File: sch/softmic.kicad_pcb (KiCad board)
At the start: 2 copper layers, 101.6 x 62.2 mm, 87 parts, among them J1 USB-C Connector, J3 XLR-OUT, J4 AudioJack 3.5mm, P1 4V1, P10 none, P2 4V1, P3 4V1, P4 4V1, P5 4V1, P6 VccPad, P7 none, P8 none, P9 none, Q1 MCP1812BT-033, Q10 ESP32-WROOM, Q11 BC847BS-TP, Q2 MMBFJ201, Q3 CH340G, Q4 BSS64AT116, Q5 OPA1671, Q6 OPA1671, Q7 BQ21040, Q8 MAX11613, Q9 Oled_128_32, SW1 RST, Y1 12MHz

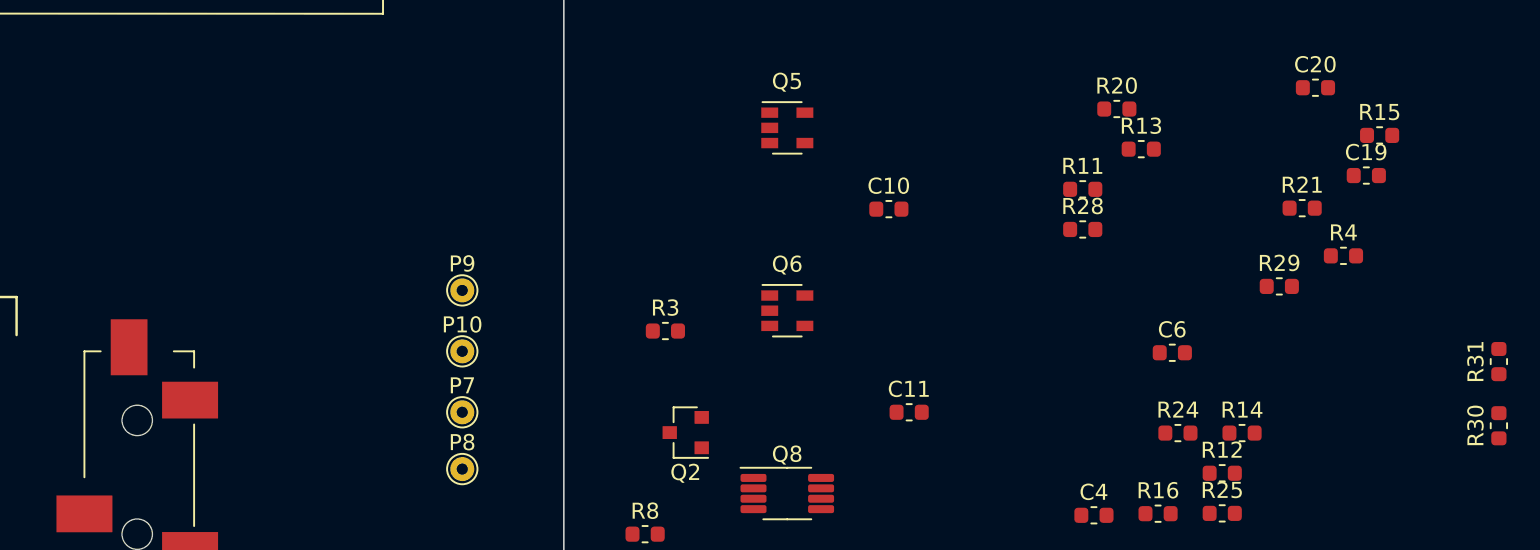
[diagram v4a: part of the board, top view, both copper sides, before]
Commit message: added small headphone volume potentiomenter
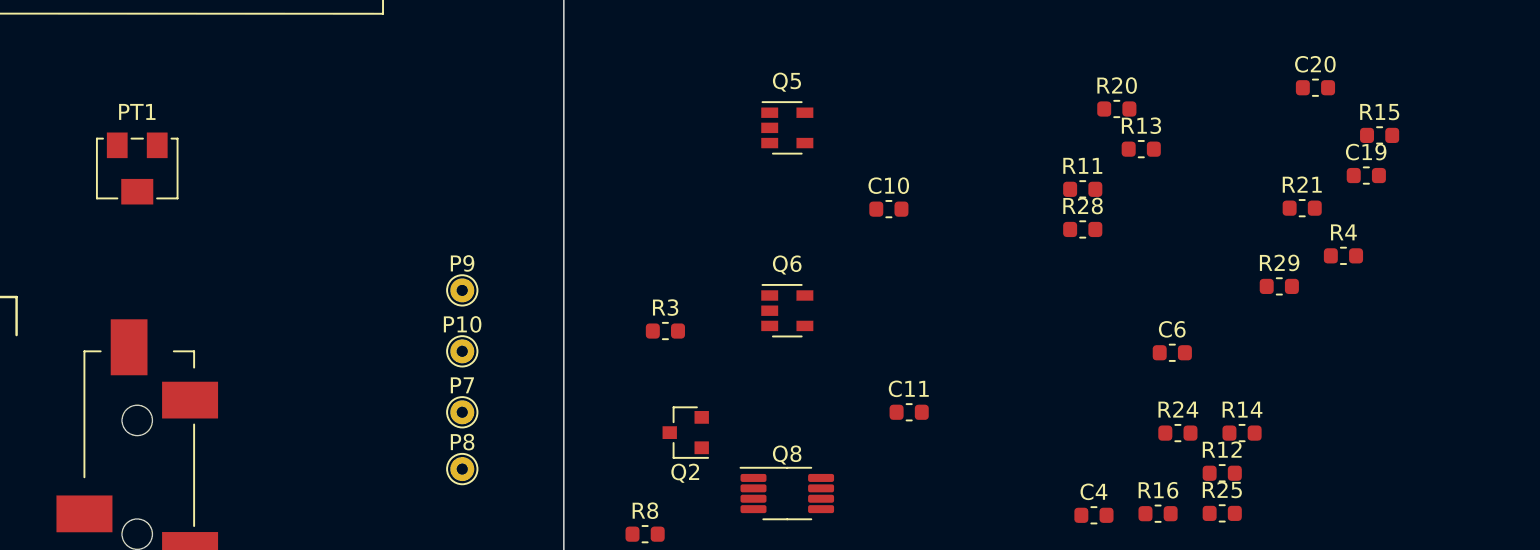
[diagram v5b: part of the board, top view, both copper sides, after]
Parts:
- removed R30, R31: 2k, Resistor_SMD:R_0603_1608Metric
- added PT1: 200k, Potentiometer_SMD:Potentiometer_Bourns_3224W_Vertical, F.Cu at (163.8, 90.2)

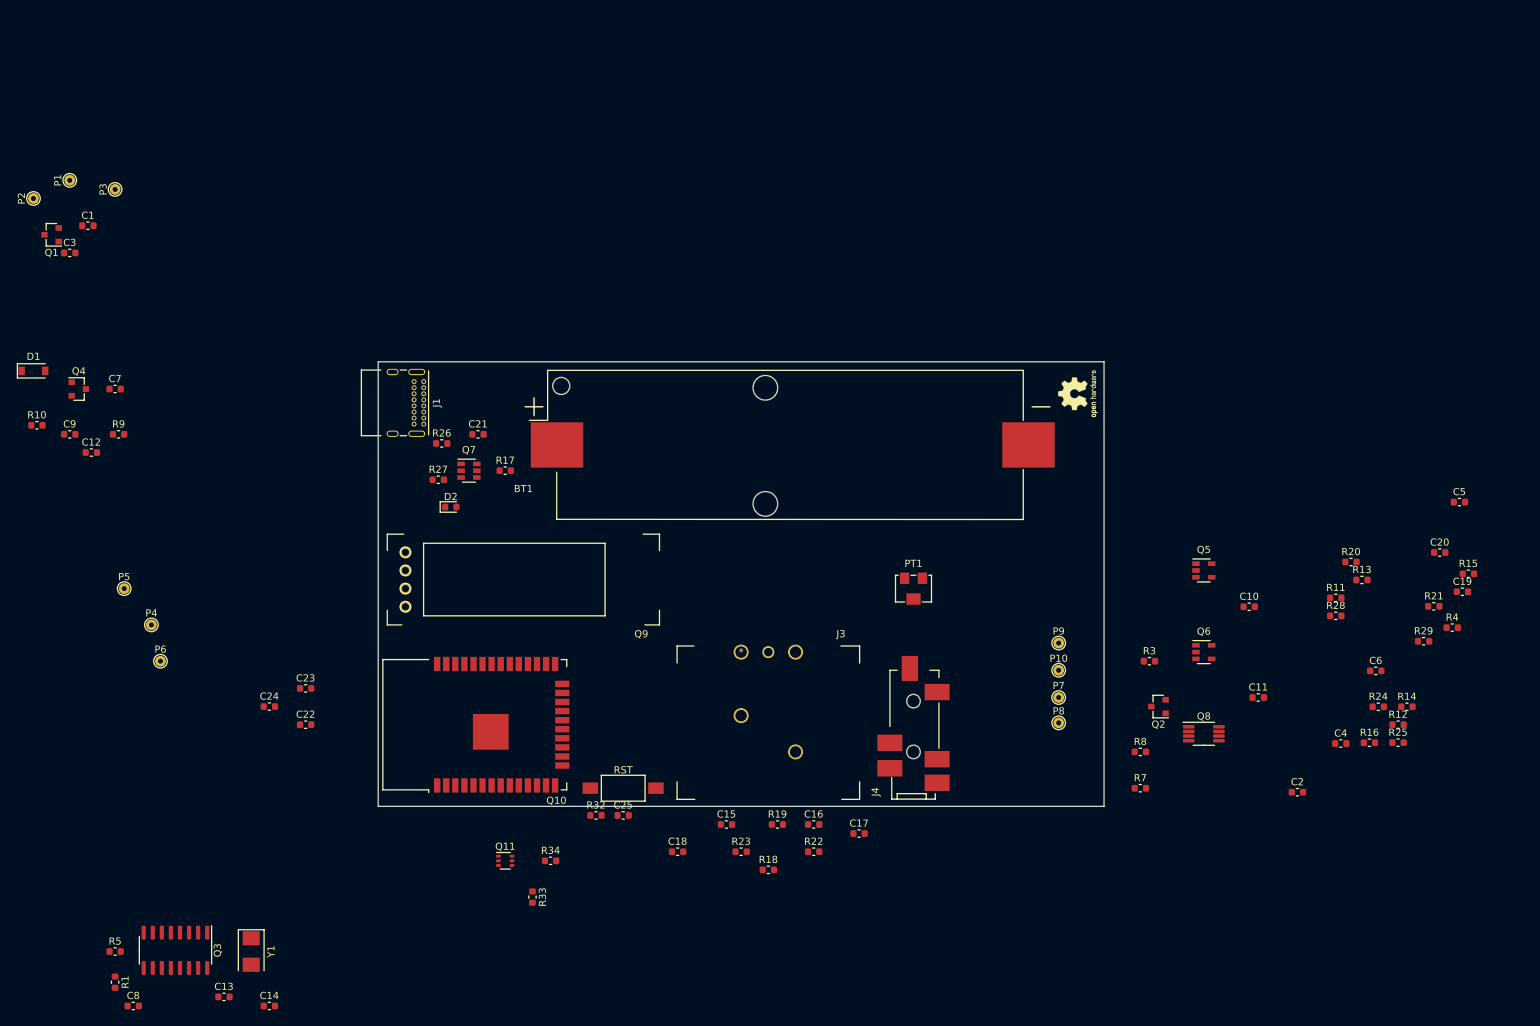
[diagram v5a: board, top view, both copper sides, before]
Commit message: changed all resistors to 0805 case resistors
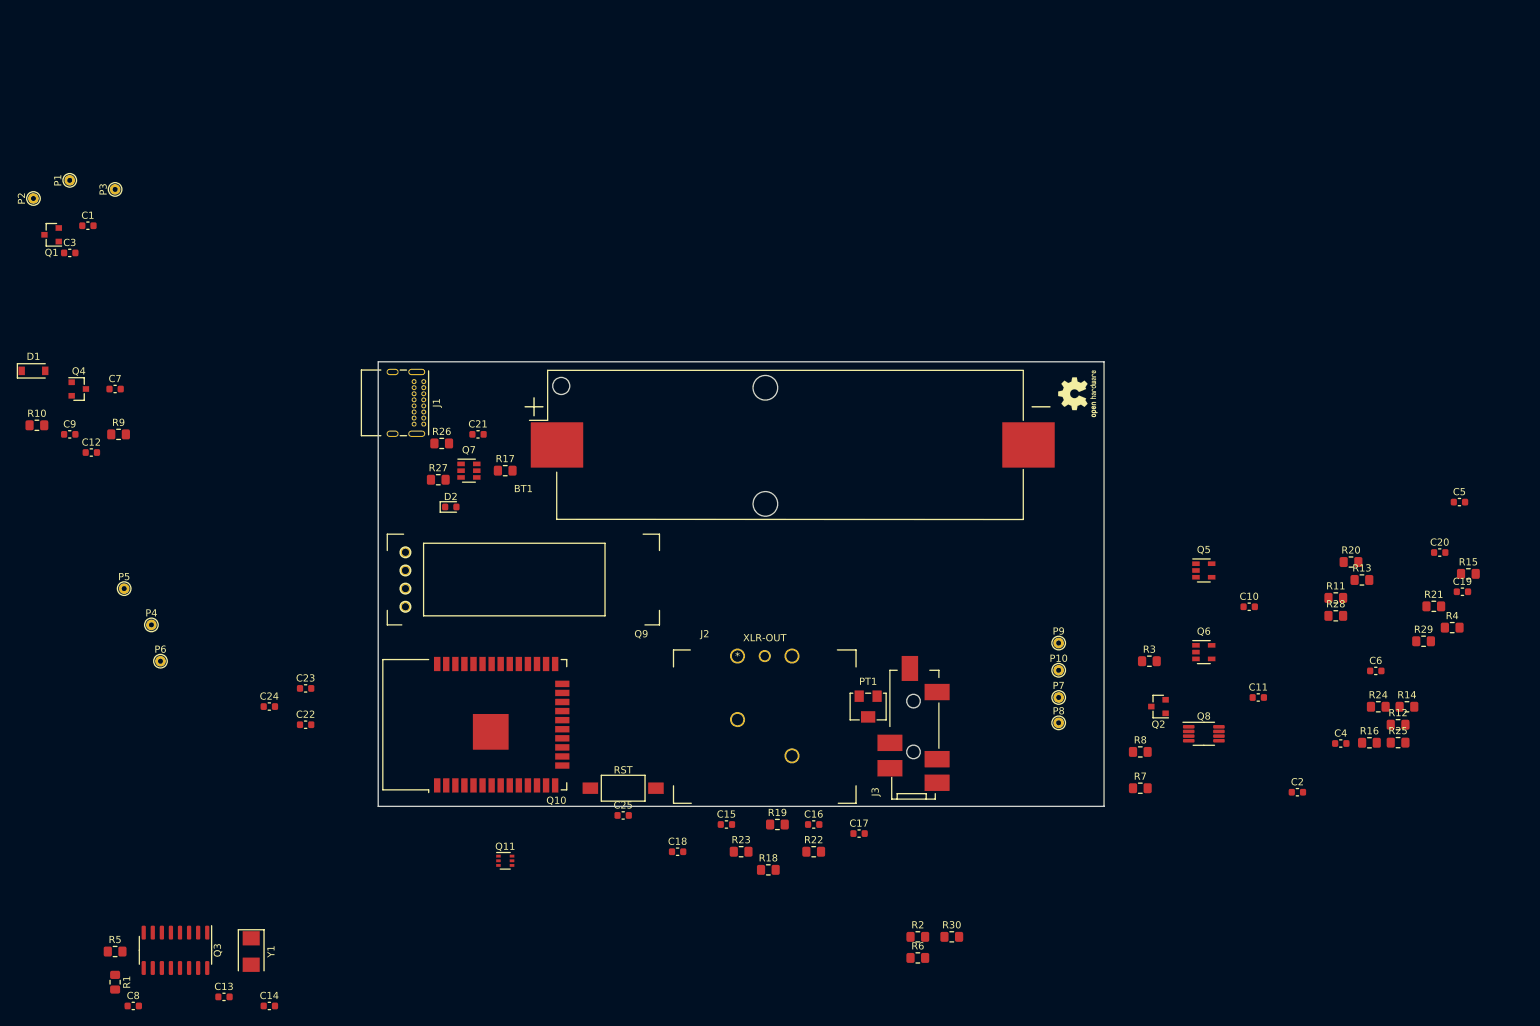
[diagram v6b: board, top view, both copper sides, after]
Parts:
- removed J4: AudioJack 3.5mm, footprint:SJ-43514-SM
- removed R32, R33, R34: 10k, Resistor_SMD:R_0603_1608Metric
- added J2: XLR-OUT, footprint:XLR-NC3MAAH-1, F.Cu at (139.2, 99.6)
- added R2: 1000k, Resistor_SMD:R_0805_2012Metric_Pad1.15x1.40mm_HandSolder, F.Cu at (164.4, 138.9)
- added R30: 10k, Resistor_SMD:R_0805_2012Metric_Pad1.15x1.40mm_HandSolder, F.Cu at (169.2, 138.9)
- added R6: 453, Resistor_SMD:R_0805_2012Metric_Pad1.15x1.40mm_HandSolder, F.Cu at (164.4, 141.9)
- C10, C14: value 1u -> 47u
- C12, C7: value 47u -> 1u
- C8: value 22p -> 47u
- C9: value 47u -> 22p
- J3: value XLR-OUT -> AudioJack 3.5mm; footprint footprint:XLR-NC3MAAH-1 -> footprint:SJ-43514-SM
- P10: value none -> VccPad
- P4, P5: value 4V1 -> none
- P6: value VccPad -> none
- P8, P9: value none -> 4V1
- R1, R14, R25: footprint Resistor_SMD:R_0603_1608Metric -> Resistor_SMD:R_0805_2012Metric_Pad1.15x1.40mm_HandSolder
- R10: value 1 -> 422k; footprint Resistor_SMD:R_0603_1608Metric -> Resistor_SMD:R_0805_2012Metric_Pad1.15x1.40mm_HandSolder
- R11: value 11k -> 18k; footprint Resistor_SMD:R_0603_1608Metric -> Resistor_SMD:R_0805_2012Metric_Pad1.15x1.40mm_HandSolder
- R12: value 422k -> 11k; footprint Resistor_SMD:R_0603_1608Metric -> Resistor_SMD:R_0805_2012Metric_Pad1.15x1.40mm_HandSolder
- R13: value 18k -> 12k; footprint Resistor_SMD:R_0603_1608Metric -> Resistor_SMD:R_0805_2012Metric_Pad1.15x1.40mm_HandSolder
- R15: value 12k -> 1k; footprint Resistor_SMD:R_0603_1608Metric -> Resistor_SMD:R_0805_2012Metric_Pad1.15x1.40mm_HandSolder
- R16: value 11k -> 47; footprint Resistor_SMD:R_0603_1608Metric -> Resistor_SMD:R_0805_2012Metric_Pad1.15x1.40mm_HandSolder
- R17: value 1k -> 47; footprint Resistor_SMD:R_0603_1608Metric -> Resistor_SMD:R_0805_2012Metric_Pad1.15x1.40mm_HandSolder
- R18: value 47 -> 180k; footprint Resistor_SMD:R_0603_1608Metric -> Resistor_SMD:R_0805_2012Metric_Pad1.15x1.40mm_HandSolder
- R19: value 47 -> 169k; footprint Resistor_SMD:R_0603_1608Metric -> Resistor_SMD:R_0805_2012Metric_Pad1.15x1.40mm_HandSolder
- R20: value 180k -> 100k; footprint Resistor_SMD:R_0603_1608Metric -> Resistor_SMD:R_0805_2012Metric_Pad1.15x1.40mm_HandSolder
- R21: value 169k -> 100k; footprint Resistor_SMD:R_0603_1608Metric -> Resistor_SMD:R_0805_2012Metric_Pad1.15x1.40mm_HandSolder
- R22, R23: value 100k -> 1k; footprint Resistor_SMD:R_0603_1608Metric -> Resistor_SMD:R_0805_2012Metric_Pad1.15x1.40mm_HandSolder
- R24: value 1k -> 10k; footprint Resistor_SMD:R_0603_1608Metric -> Resistor_SMD:R_0805_2012Metric_Pad1.15x1.40mm_HandSolder
- R26: value 10k -> 200k; footprint Resistor_SMD:R_0603_1608Metric -> Resistor_SMD:R_0805_2012Metric_Pad1.15x1.40mm_HandSolder
- R27: value 1k -> 200k; footprint Resistor_SMD:R_0603_1608Metric -> Resistor_SMD:R_0805_2012Metric_Pad1.15x1.40mm_HandSolder
- R28, R29: value 200k -> 10k; footprint Resistor_SMD:R_0603_1608Metric -> Resistor_SMD:R_0805_2012Metric_Pad1.15x1.40mm_HandSolder
- R3: value 1000k -> 1k; footprint Resistor_SMD:R_0603_1608Metric -> Resistor_SMD:R_0805_2012Metric_Pad1.15x1.40mm_HandSolder
- R4: value 1k -> 470; footprint Resistor_SMD:R_0603_1608Metric -> Resistor_SMD:R_0805_2012Metric_Pad1.15x1.40mm_HandSolder
- R5: value 470 -> 2k; footprint Resistor_SMD:R_0603_1608Metric -> Resistor_SMD:R_0805_2012Metric_Pad1.15x1.40mm_HandSolder
- R7: value 2k -> 340; footprint Resistor_SMD:R_0603_1608Metric -> Resistor_SMD:R_0805_2012Metric_Pad1.15x1.40mm_HandSolder
- R8: value 453 -> 1; footprint Resistor_SMD:R_0603_1608Metric -> Resistor_SMD:R_0805_2012Metric_Pad1.15x1.40mm_HandSolder
- R9: value 340 -> 11k; footprint Resistor_SMD:R_0603_1608Metric -> Resistor_SMD:R_0805_2012Metric_Pad1.15x1.40mm_HandSolder
- moved J3 25.7 mm to (163.8, 108.0), turned to 90 degrees
- moved PT1 17.7 mm to (157.5, 106.7)
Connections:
- C10 pad 1: Net-(C10-Pad1) -> /4V1
- C10 pad 2: /JFET_OUT -> GND
- C12 pad 1: /4V1 -> Net-(C12-Pad1)
- C12 pad 2: GND -> /JFET_OUT
- C14 pad 1: GND -> /4V1
- C14 pad 2: +3V3 -> GND
- C4 pad 2: /Vcc -> +3V3
- C7 pad 1: Net-(C7-Pad1) -> GND
- C7 pad 2: GND -> /Vcc
- C8 pad 1: /XI -> Net-(C8-Pad1)
- C9 pad 1: /4V1 -> /XI
- D1 pad 1: Net-(C7-Pad1) -> Net-(C8-Pad1)
- P10 pad 1: GND -> Net-(P10-Pad1)
- P4 pad 1: /BATT -> /JFET_OUT
- P5 pad 1: /4V1 -> GND
- P6 pad 1: Net-(P6-Pad1) -> /MIC-IN1
- P7 pad 1: /JFET_OUT -> GND
- P8 pad 1: GND -> /BATT
- P9 pad 1: /MIC-IN1 -> /4V1
- PT1 pad 2: Net-(J4-PadR) -> Net-(J3-PadR)
- Q4 pad 2: Net-(C7-Pad1) -> Net-(C8-Pad1)
- Q6 pad 3: Net-(C11-Pad1) -> Net-(C12-Pad1)
- R10 pad 1: /4V1 -> /Vcc
- R10 pad 2: Net-(Q4-Pad1) -> Net-(C12-Pad1)
- R11 pad 1: Net-(C11-Pad1) -> /Vcc
- R11 pad 2: GND -> Net-(Q5-Pad3)
- R12 pad 1: /Vcc -> Net-(Q5-Pad4)
- R13 pad 1: /Vcc -> Net-(Q5-Pad3)
- R13 pad 2: Net-(Q5-Pad3) -> GND
- R14 pad 1: Net-(Q5-Pad4) -> Net-(Q6-Pad4)
- R14 pad 2: Net-(C10-Pad1) -> GND
- R15 pad 1: Net-(Q5-Pad3) -> GND
- R15 pad 2: GND -> Net-(Q7-Pad4)
- R16 pad 1: Net-(Q6-Pad4) -> Net-(C15-Pad1)
- R16 pad 2: GND -> Net-(C17-Pad2)
- R17 pad 1: GND -> Net-(C16-Pad1)
- R17 pad 2: Net-(Q7-Pad4) -> Net-(C18-Pad1)
- R18 pad 1: Net-(C15-Pad1) -> Net-(Q5-Pad1)
- R18 pad 2: Net-(C17-Pad2) -> Net-(Q5-Pad4)
- R19 pad 1: Net-(C16-Pad1) -> Net-(Q6-Pad1)
- R19 pad 2: Net-(C18-Pad1) -> Net-(Q6-Pad4)
- R20 pad 1: Net-(Q5-Pad1) -> Net-(C17-Pad2)
- R20 pad 2: Net-(Q5-Pad4) -> GND
- R21 pad 1: Net-(Q6-Pad1) -> GND
- R21 pad 2: Net-(Q6-Pad4) -> Net-(C18-Pad1)
- R22 pad 1: Net-(C17-Pad2) -> /OUT1
- R22 pad 2: GND -> Net-(Q5-Pad1)
- R23 pad 1: GND -> /OUT2
- R23 pad 2: Net-(C18-Pad1) -> Net-(Q6-Pad1)
- R24 pad 1: /OUT1 -> GND
- R24 pad 2: Net-(Q5-Pad1) -> Net-(Q7-Pad1)
- R25 pad 1: /OUT2 -> Net-(D2-Pad1)
- R25 pad 2: Net-(Q6-Pad1) -> Net-(Q7-Pad3)
- R26 pad 2: Net-(Q7-Pad1) -> /OUT1
- R27 pad 1: Net-(D2-Pad1) -> GND
- R27 pad 2: Net-(Q7-Pad3) -> /OUT2
- R28 pad 1: GND -> +3V3
- R28 pad 2: /OUT1 -> /ESP_EN
- R29 pad 1: GND -> /RTS
- R29 pad 2: /OUT2 -> Net-(Q11-Pad2)
- R3 pad 1: GND -> /Vcc
- R3 pad 2: /MIC-IN1 -> Net-(P10-Pad1)
- R4 pad 1: /Vcc -> Net-(J1-PadA7)
- R4 pad 2: Net-(P6-Pad1) -> Net-(Q3-Pad6)
- R5 pad 1: Net-(J1-PadA7) -> /JFET_OUT
- R5 pad 2: Net-(Q3-Pad6) -> /Vcc
- R7 pad 1: /JFET_OUT -> Net-(C8-Pad1)
- R7 pad 2: /Vcc -> +5V
- R8 pad 1: GND -> /4V1
- R8 pad 2: Net-(Q2-Pad3) -> Net-(Q4-Pad1)
- R9 pad 1: Net-(C7-Pad1) -> Net-(C12-Pad1)
- R9 pad 2: +5V -> GND

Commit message: change all caps to 0805 case caps
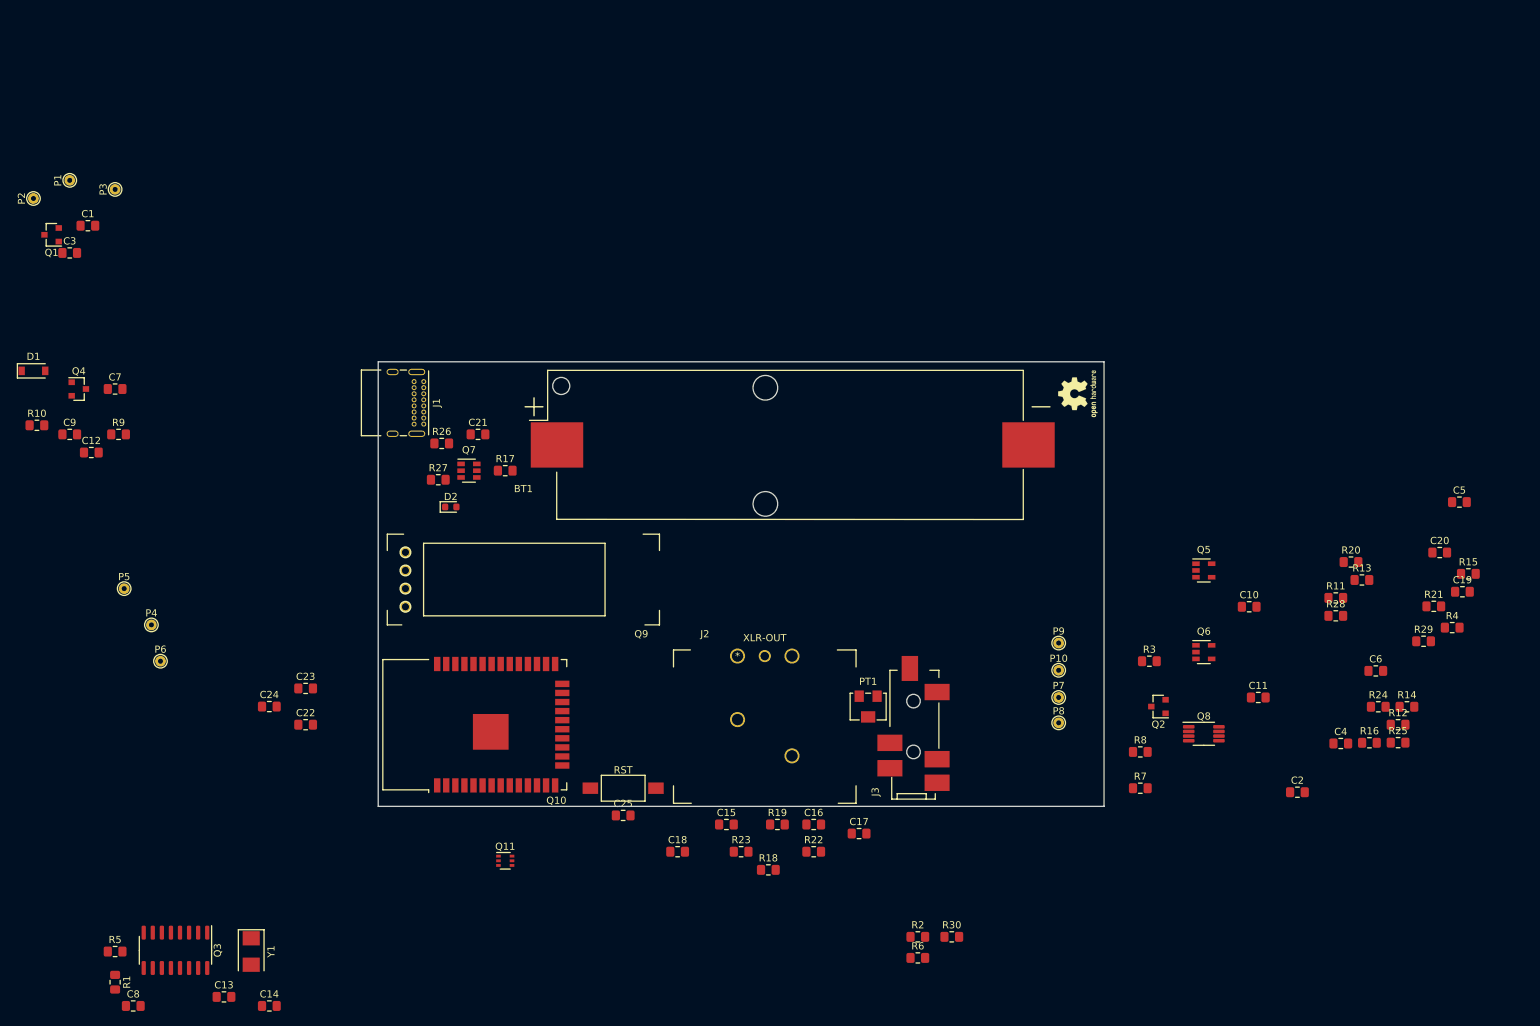
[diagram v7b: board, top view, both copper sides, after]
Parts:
- C1, C10, C11, C12, C13, C14, C15, C16, C17, C18, C19, C2, C20, C21, C22, C23, C24, C25, C3, C4, C5, C6, C7, C8, C9: footprint Capacitor_SMD:C_0603_1608Metric -> Capacitor_SMD:C_0805_2012Metric_Pad1.15x1.40mm_HandSolder
